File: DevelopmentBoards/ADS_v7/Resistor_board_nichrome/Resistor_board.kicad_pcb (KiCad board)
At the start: 2 copper layers, 39 x 12.8 mm, 6 parts, among them J1 Conn_01x06_Pin, SW1 SW_SPDT_312

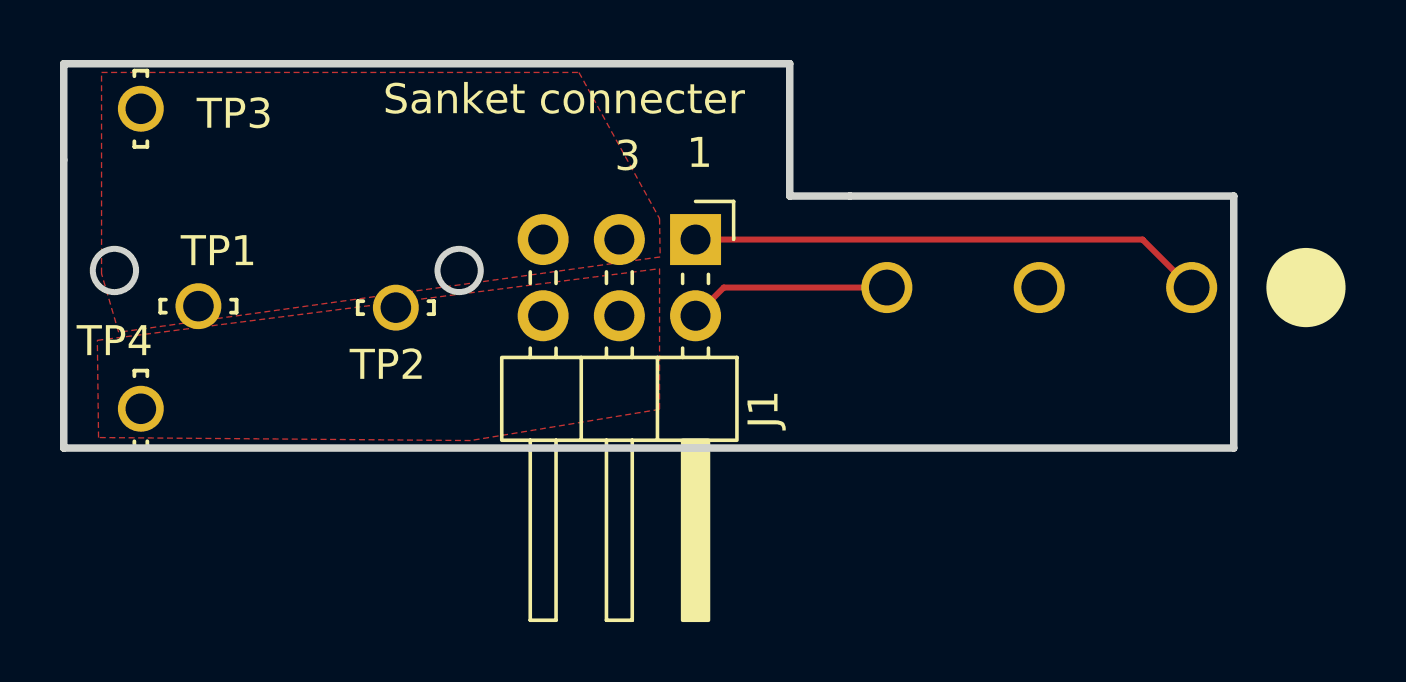
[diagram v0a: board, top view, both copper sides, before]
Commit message: Corrected board settings for resistor and nichrome boards also. Replaced pour to thick copper trace on resistor and nichrome boards
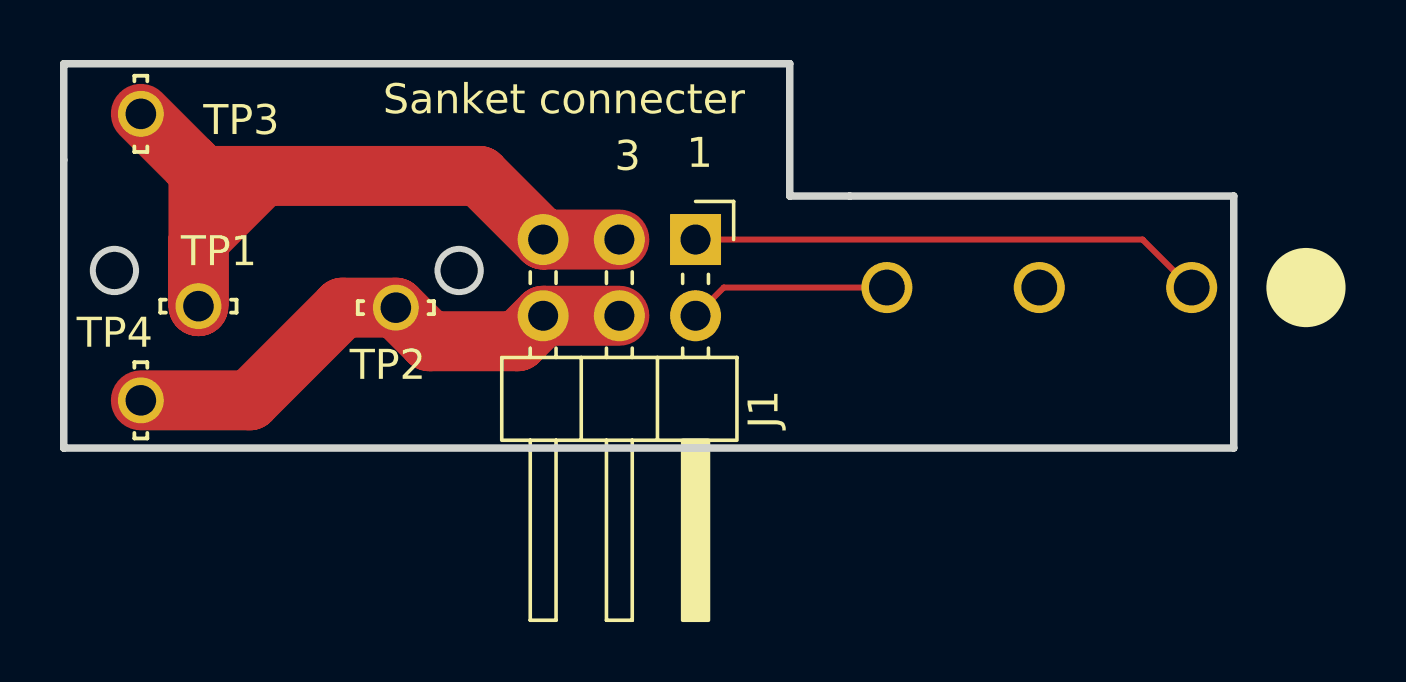
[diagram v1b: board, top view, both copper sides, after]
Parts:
- moved TP4 0.28 mm to (112.5, 62.7)
- moved TP3 0.17 mm to (112.5, 53.1)
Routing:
- net /BurnWireIN: track 0.00 -> 27.4 mm
- net /GND: track 0.00 -> 18.0 mm
- removed copper zone on F.Cu, net /BurnWireIN
- removed copper zone on F.Cu, net /GND
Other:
- board text removed: "Testpoints"
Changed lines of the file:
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@@
 	(footprint "5021:TP_5021"
 		(layer "F.Cu")
-		(at 112.51 52.94 -90)
+		(at 112.51 53.11 -90)
 		(property "Reference" "TP3"
-			(at 0.17 -3.13 180)
+			(at 0.21 -3.35 180)
 			(layer "F.SilkS")
 			(effects
@@
 	(footprint "5021:TP_5021"
 		(layer "F.Cu")
-		(at 112.51 62.94 -90)
+		(at 112.51 62.66 -90)
 		(property "Reference" "TP4"
 			(at -2.25 0.87 180)
@@
 		)
 	)
-	(gr_text "Testpoints\n"
-		(at 127 56.8 0)
-		(layer "B.SilkS")
-		(effects
-			(font
-				(size 1 1)
-				(thickness 0.1)
-			)
-			(justify left bottom mirror)
-		)
-	)
 	(gr_text "Switch \n"
 		(at 141.5 63.494 0)
@@
 	)
 	(segment
+		(start 114.43 57.33)
+		(end 114.43 59.52)
+		(width 2)
+		(layer "F.Cu")
+		(net "/BurnWireIN")
+	)
+	(segment
+		(start 114.8 55.4)
+		(end 114.54 55.66)
+		(width 2)
+		(layer "F.Cu")
+		(net "/BurnWireIN")
+	)
+	(segment
+		(start 123.8 55.18)
+		(end 115.01 55.18)
+		(width 2)
+		(layer "F.Cu")
+		(net "/BurnWireIN")
+	)
+	(segment
+		(start 114.21 54.81)
+		(end 114.43 55.03)
+		(width 2)
+		(layer "F.Cu")
+		(net "/BurnWireIN")
+	)
+	(segment
+		(start 128.46 57.3)
+		(end 125.92 57.3)
+		(width 2)
+		(layer "F.Cu")
+		(net "/BurnWireIN")
+	)
+	(segment
+		(start 114.8 55.39)
+		(end 114.8 55.4)
+		(width 2)
+		(layer "F.Cu")
+		(net "/BurnWireIN")
+	)
+	(segment
+		(start 114.43 55.03)
+		(end 114.43 59.52)
+		(width 2)
+		(layer "F.Cu")
+		(net "/BurnWireIN")
+	)
+	(segment
+		(start 112.51 53.11)
+		(end 114.21 54.81)
+		(width 2)
+		(layer "F.Cu")
+		(net "/BurnWireIN")
+	)
+	(segment
+		(start 125.92 57.3)
+		(end 123.8 55.18)
+		(width 2)
+		(layer "F.Cu")
+		(net "/BurnWireIN")
+	)
+	(segment
+		(start 115.01 55.18)
+		(end 114.8 55.39)
+		(width 2)
+		(layer "F.Cu")
+		(net "/BurnWireIN")
+	)
+	(segment
+		(start 116.58 55.18)
+		(end 114.43 57.33)
+		(width 2)
+		(layer "F.Cu")
+		(net "/BurnWireIN")
+	)
+	(segment
+		(start 121.01 59.57)
+		(end 119.23 59.57)
+		(width 2)
+		(layer "F.Cu")
+		(net "/GND")
+	)
+	(segment
+		(start 119.23 59.57)
+		(end 116.14 62.66)
+		(width 2)
+		(layer "F.Cu")
+		(net "/GND")
+	)
+	(segment
+		(start 125.07 60.69)
+		(end 122.13 60.69)
+		(width 2)
+		(layer "F.Cu")
+		(net "/GND")
+	)
+	(segment
+		(start 128.46 59.84)
+		(end 125.92 59.84)
+		(width 2)
+		(layer "F.Cu")
+		(net "/GND")
+	)
+	(segment
+		(start 116.14 62.66)
+		(end 112.51 62.66)
+		(width 2)
+		(layer "F.Cu")
+		(net "/GND")
+	)
+	(segment
+		(start 125.92 59.84)
+		(end 125.07 60.69)
+		(width 2)
+		(layer "F.Cu")
+		(net "/GND")
+	)
+	(segment
+		(start 122.13 60.69)
+		(end 121.01 59.57)
+		(width 2)
+		(layer "F.Cu")
+		(net "/GND")
+	)
+	(segment
 		(start 131 57.3)
 		(end 145.9 57.3)
@@
 	)
 	(zone
+		(net "/DeployerDetectionSWOUT")
+		(layer "F.Cu")
+		(hatch none 0.1)
+		(priority 30002)
+		(attr
+			(teardrop
+				(type padvia)
+			)
+		)
+		(connect_pads yes
+			(clearance 0)
+		)
+		(min_thickness 0.0254)
+		(fill yes
+			(island_removal_mode 1)
+		)
+		(polygon
+			(pts
+				(xy 146.388954 57.647533) (xy 146.247533 57.788954) (xy 146.723139 59.147003) (xy 147.522304 58.922304)
+				(xy 147.784403 58.085739)
+			)
+		)
+	)
+	(zone
 		(net "/DeployerDetectionSWIN")
 		(layer "F.Cu")
@@
 			)
 		)
-	)
-	(zone
-		(net "/BurnWireIN")
-		(layer "F.Cu")
-		(hatch full 0.5)
-		(connect_pads
-			(clearance 0.5)
-		)
-		(min_thickness 0.25)
-		(fill yes
-			(thermal_gap 0.5)
-			(thermal_bridge_width 0.5)
-			(island_removal_mode 0)
-		)
-		(polygon
-			(pts
-				(xy 111.2 51.73) (xy 127.113103 51.73) (xy 129.8 56.6) (xy 129.82 57.88) (xy 111.77 60.39) (xy 111.2 58.436846)
-			)
-		)
-	)
-	(zone
-		(net "/DeployerDetectionSWOUT")
-		(layer "F.Cu")
-		(hatch none 0.1)
-		(priority 30002)
-		(attr
-			(teardrop
-				(type padvia)
-			)
-		)
-		(connect_pads yes
-			(clearance 0)
-		)
-		(min_thickness 0.0254)
-		(fill yes
-			(island_removal_mode 1)
-		)
-		(polygon
-			(pts
-				(xy 146.388954 57.647533) (xy 146.247533 57.788954) (xy 146.723139 59.147003) (xy 147.522304 58.922304)
-				(xy 147.784403 58.085739)
-			)
-		)
-	)
-	(zone
-		(net "/GND")
-		(layer "F.Cu")
-		(hatch full 0.5)
-		(priority 1)
-		(connect_pads
-			(clearance 0.5)
-		)
-		(min_thickness 0.25)
-		(fill yes
-			(thermal_gap 0.5)
-			(thermal_bridge_width 0.5)
-			(island_removal_mode 0)
-		)
-		(polygon
-			(pts
-				(xy 111.06 60.66) (xy 129.8 58.271219) (xy 129.8 62.96) (xy 123.5 64) (xy 111.1 63.9)
-			)
-		)

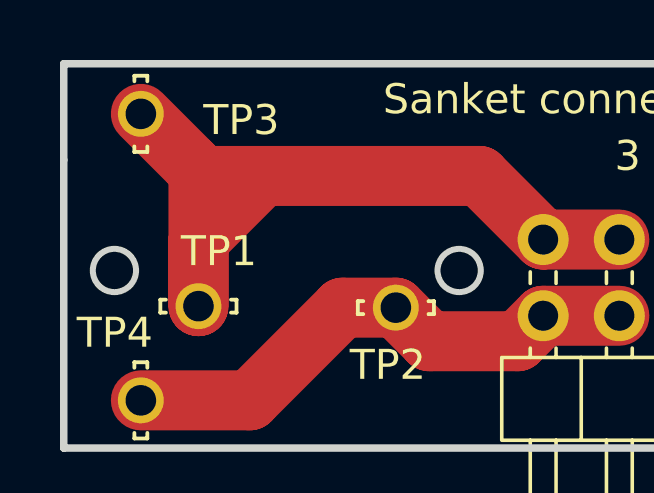
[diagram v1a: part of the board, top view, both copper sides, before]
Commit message: ADS v7: Corrected layout of converter, replaced tp pads with thp pads in resistor board, some other minor trace layout changes
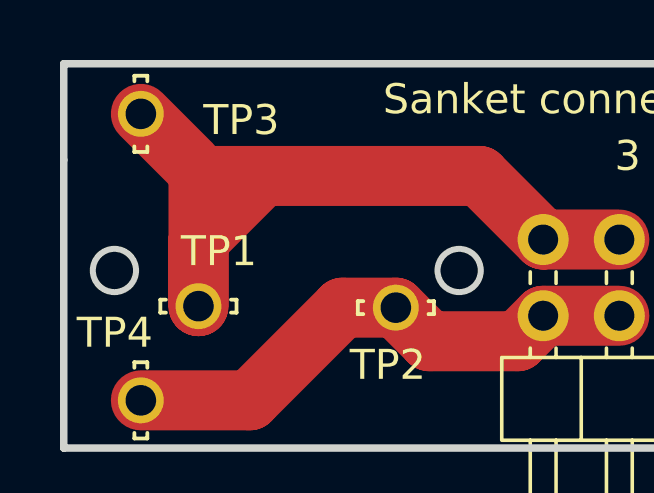
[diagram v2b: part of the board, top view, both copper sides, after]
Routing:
- net /BurnWireIN: track 27.4 -> 26.5 mm
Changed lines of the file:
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@@
-	)
-	(segment
-		(start 114.8 55.4)
-		(end 114.54 55.66)
-		(width 2)
-		(layer "F.Cu")
-		(net "/BurnWireIN")
 	)
 	(segment
@@
 	)
 	(segment
-		(start 114.21 54.81)
-		(end 114.43 55.03)
-		(width 2)
-		(layer "F.Cu")
-		(net "/BurnWireIN")
-	)
-	(segment
 		(start 128.46 57.3)
 		(end 125.92 57.3)
-		(width 2)
-		(layer "F.Cu")
-		(net "/BurnWireIN")
-	)
-	(segment
-		(start 114.8 55.39)
-		(end 114.8 55.4)
 		(width 2)
 		(layer "F.Cu")
@@
 		(width 2)
 		(layer "F.Cu")
-		(net "/BurnWireIN")
-	)
-	(segment
-		(start 115.01 55.18)
-		(end 114.8 55.39)
-		(width 2)
-		(layer "F.Cu")
